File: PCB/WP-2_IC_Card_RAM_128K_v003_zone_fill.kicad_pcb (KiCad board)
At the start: 2 copper layers, 14.5 x 48.5 mm, 8 parts, among them J1 Conn_01x38_Female, U1 SRAM 128Kx8 5v Parallel, U2 SRAM 128Kx8 5v Parallel

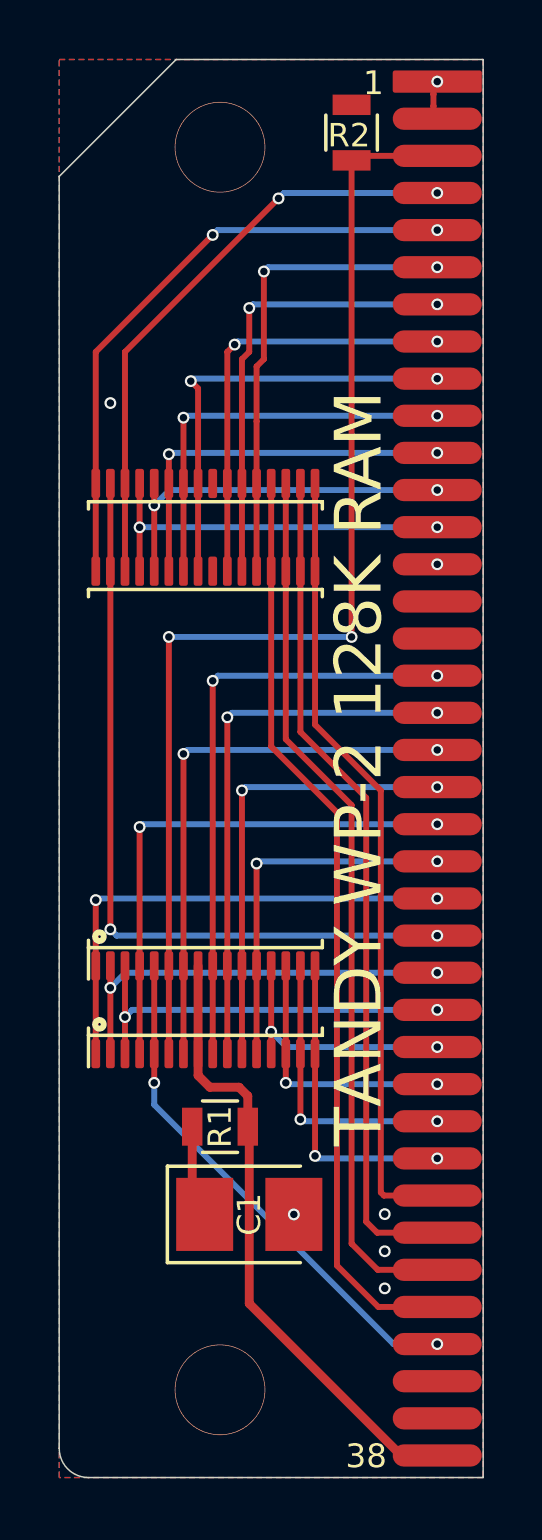
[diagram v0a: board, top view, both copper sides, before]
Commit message: better silkscreen on v003, pics, prep v003 w/zone will be next main version
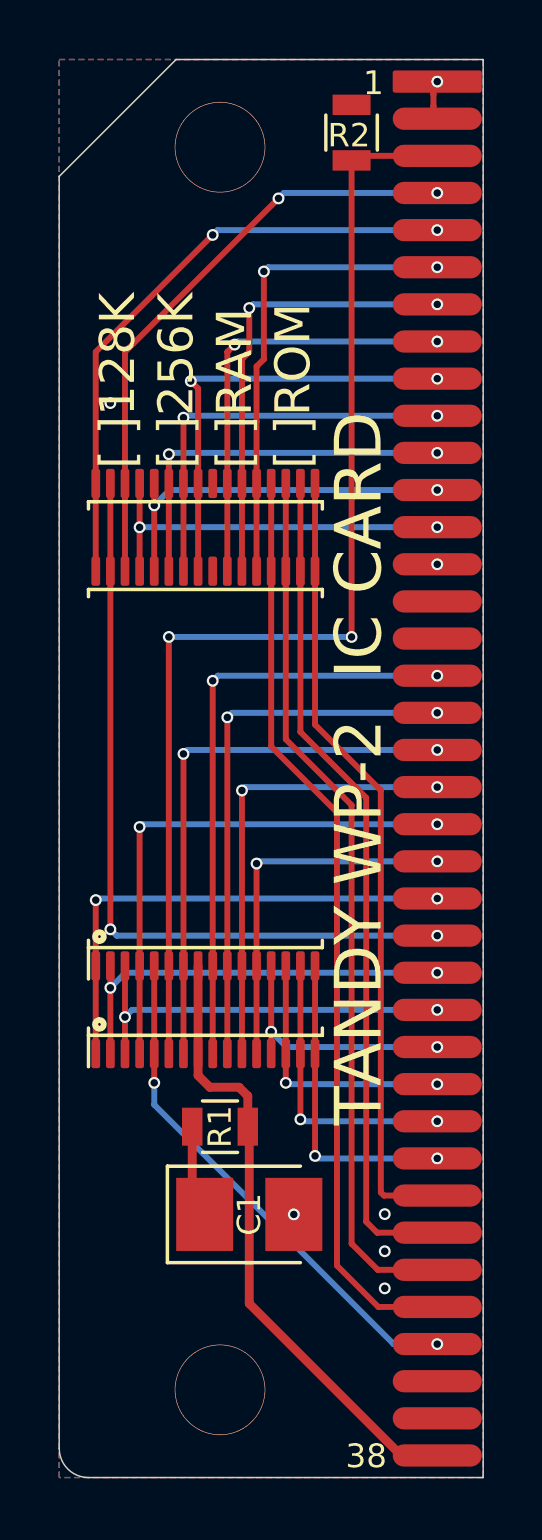
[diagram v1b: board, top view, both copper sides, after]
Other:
- board text added: "TANDY WP-2 IC CARD"
- board text added: "[ ]128K"
- board text added: "[ ]256K"
- board text added: "[ ]RAM"
- board text added: "[ ]ROM"
- board text removed: "TANDY WP-2 128K RAM"
